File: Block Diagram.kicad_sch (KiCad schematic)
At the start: 0 parts

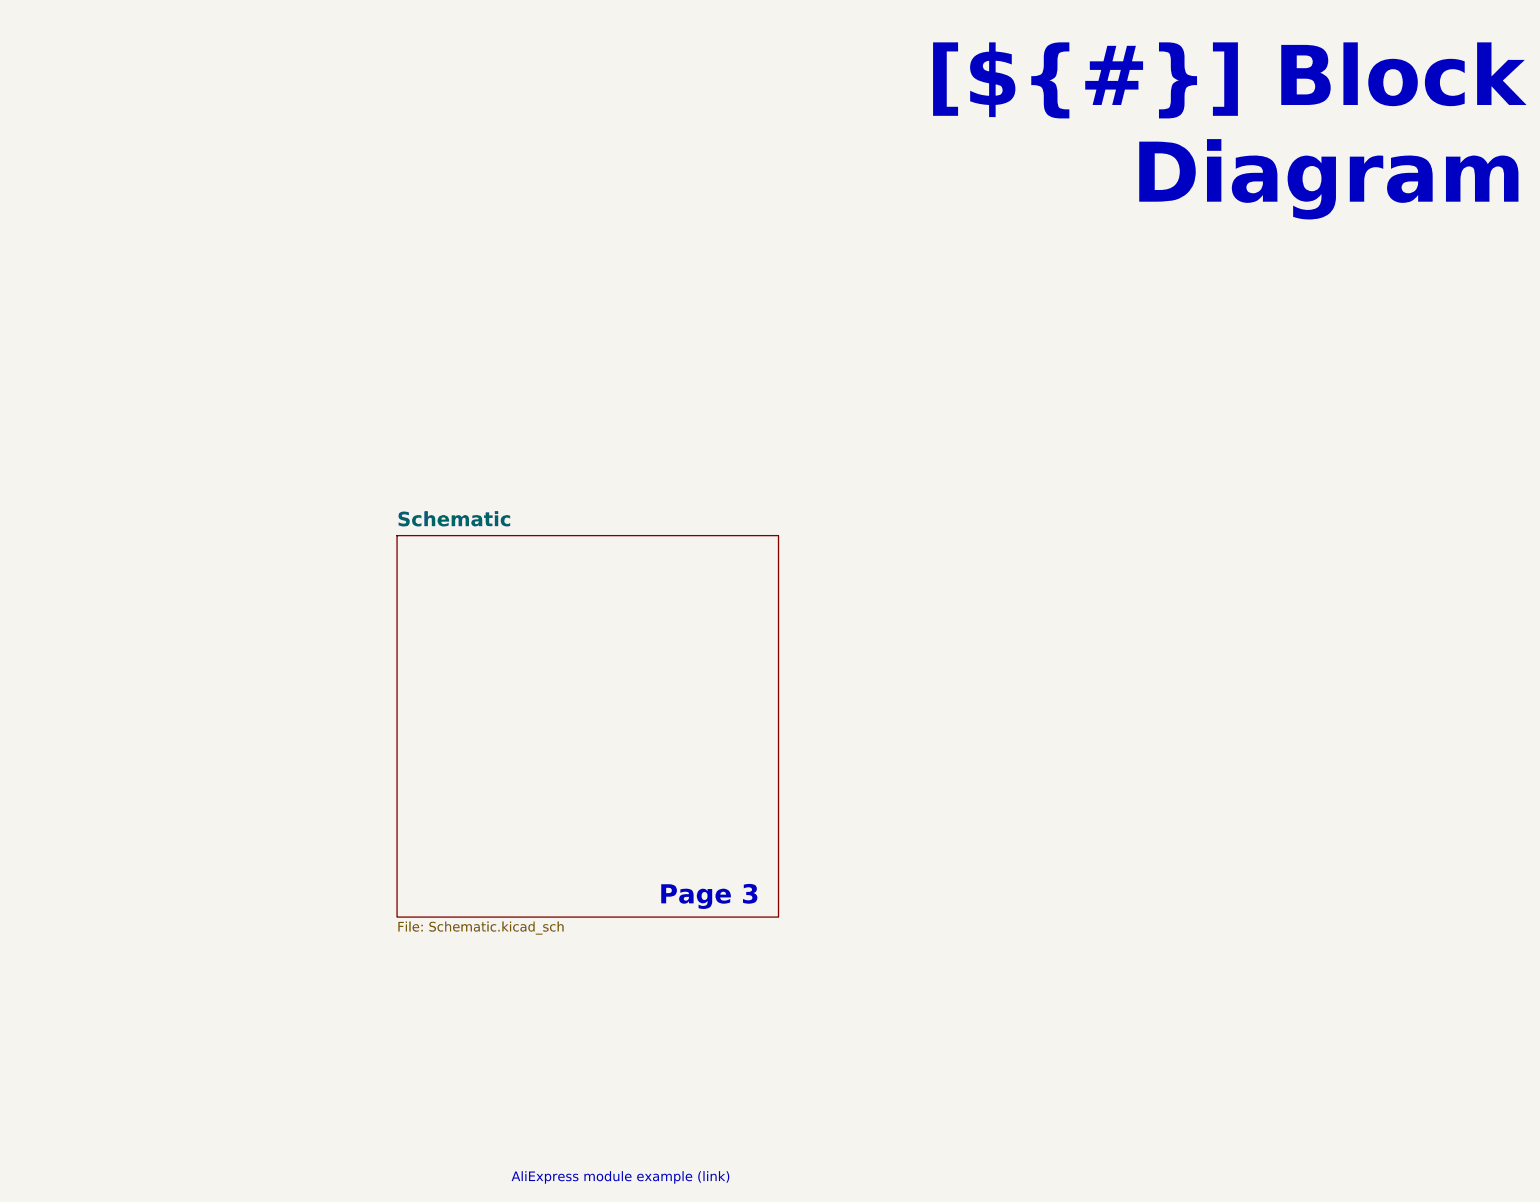
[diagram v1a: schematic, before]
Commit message: added perfboard
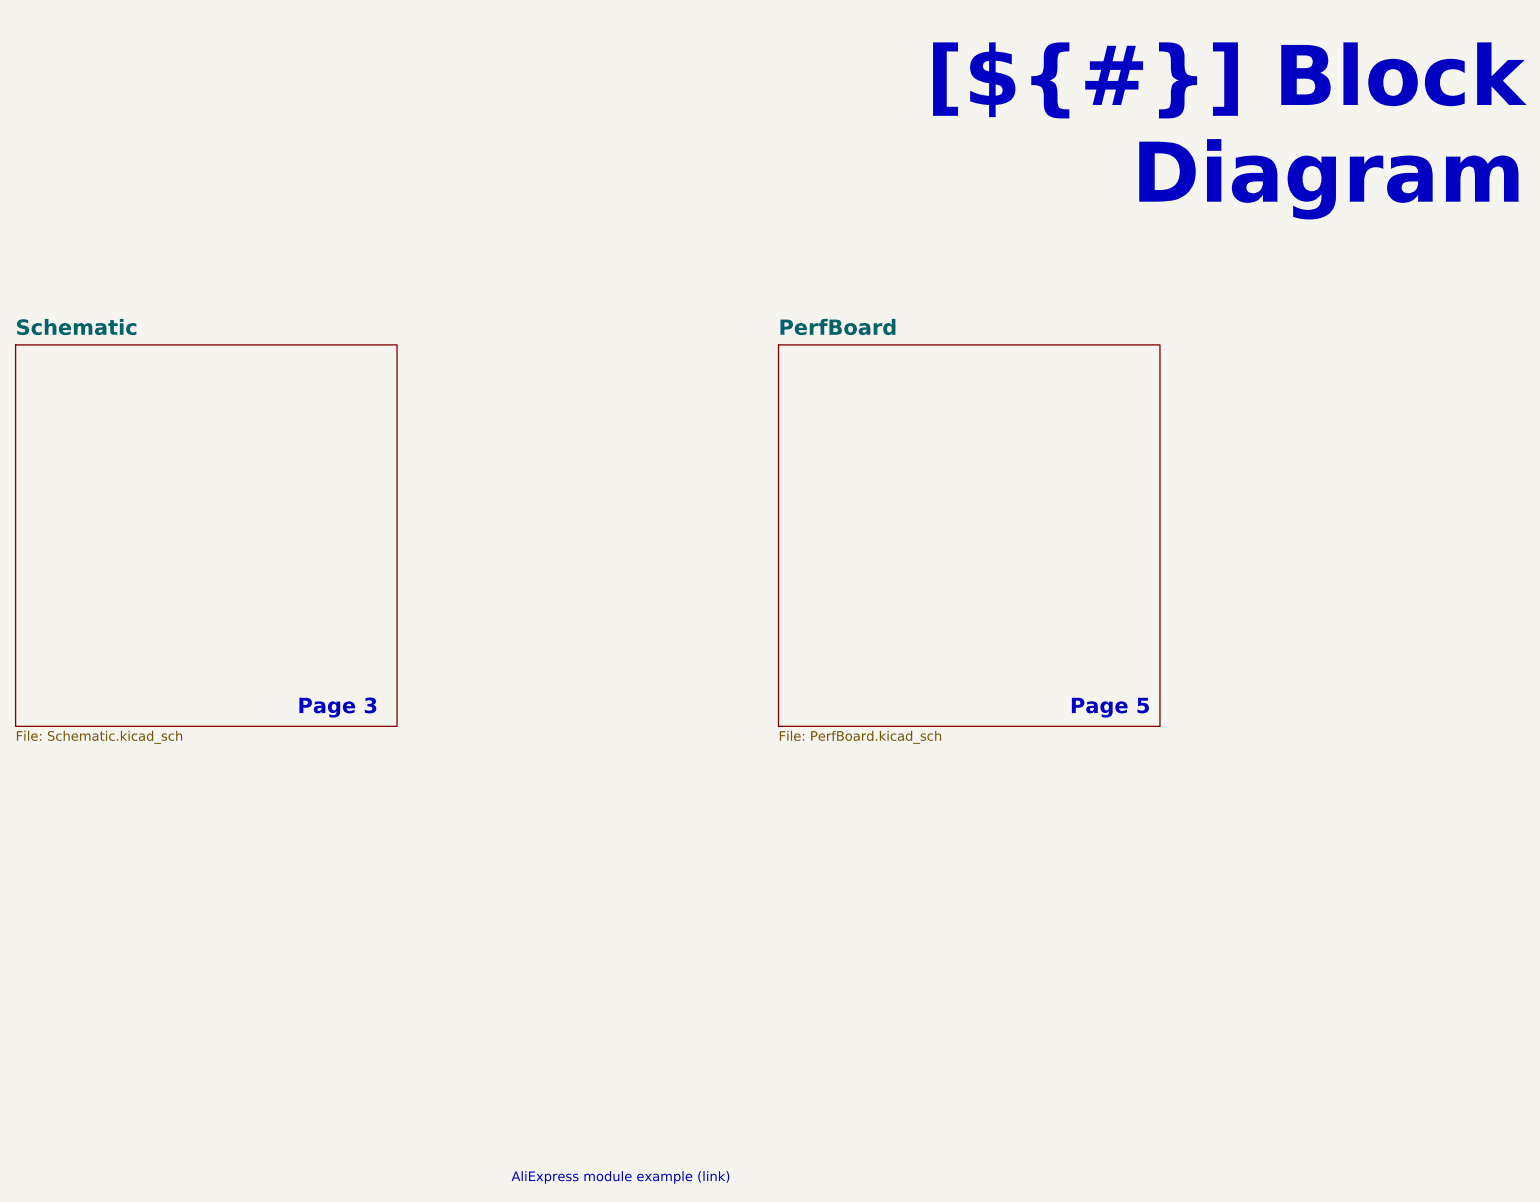
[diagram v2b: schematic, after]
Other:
- added sheet PerfBoard (PerfBoard.kicad_sch)
- note added: "Page 5"
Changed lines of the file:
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@@
 		(comment 9 "FR")
+	)
+	(text "Page 5"
+		(exclude_from_sim no)
+		(at 227.33 100.33 0)
+		(effects
+			(font
+				(size 2.032 2.032)
+				(bold yes)
+				(color 20 60 40 1)
+			)
+			(justify right bottom)
+			(href "#5")
+		)
 	)
 	(text "Page 3"
 		(exclude_from_sim no)
-		(at 175.26 125.73 0)
+		(at 124.46 100.33 0)
 		(effects
 			(font
-				(size 2.54 2.54)
+				(size 2.032 2.032)
 				(bold yes)
 				(color 20 60 40 1)
@@
 	)
 	(sheet
-		(at 127 76.2)
+		(at 177.8 50.8)
+		(size 50.8 50.8)
+		(exclude_from_sim no)
+		(in_bom yes)
+		(on_board yes)
+		(dnp no)
+		(fields_autoplaced yes)
+		(stroke
+			(width 0.1524)
+			(type solid)
+		)
+		(fill
+			(color 128 255 128 0.5020)
+		)
+		(property "Sheetname" "PerfBoard"
+			(at 177.8 49.7074 0)
+			(effects
+				(font
+					(size 2.032 2.032)
+					(thickness 0.4064)
+					(bold yes)
+				)
+				(justify left bottom)
+			)
+		)
+		(property "Sheetfile" "PerfBoard.kicad_sch"
+			(at 177.8 102.1846 0)
+			(effects
+				(font
+					(size 1.27 1.27)
+				)
+				(justify left top)
+			)
+		)
+		(instances
+			(project "Isolated_12to450V"
+				(path "/f9e05184-c88b-4a88-ae9c-ab2bdb32be7c/82da9dbf-ba38-4d08-ba35-a220fa2963b1"
+					(page "5")
+				)
+			)
+		)
+	)
+	(sheet
+		(at 76.2 50.8)
 		(size 50.8 50.8)
 		(exclude_from_sim no)
@@
 		)
 		(property "Sheetname" "Schematic"
-			(at 127 75.1709 0)
+			(at 76.2 49.7074 0)
 			(effects
 				(font
-					(size 1.905 1.905)
+					(size 2.032 2.032)
 					(bold yes)
 				)
@@
 		)
 		(property "Sheetfile" "Schematic.kicad_sch"
-			(at 127 127.5846 0)
+			(at 76.2 102.1846 0)
 			(effects
 				(font

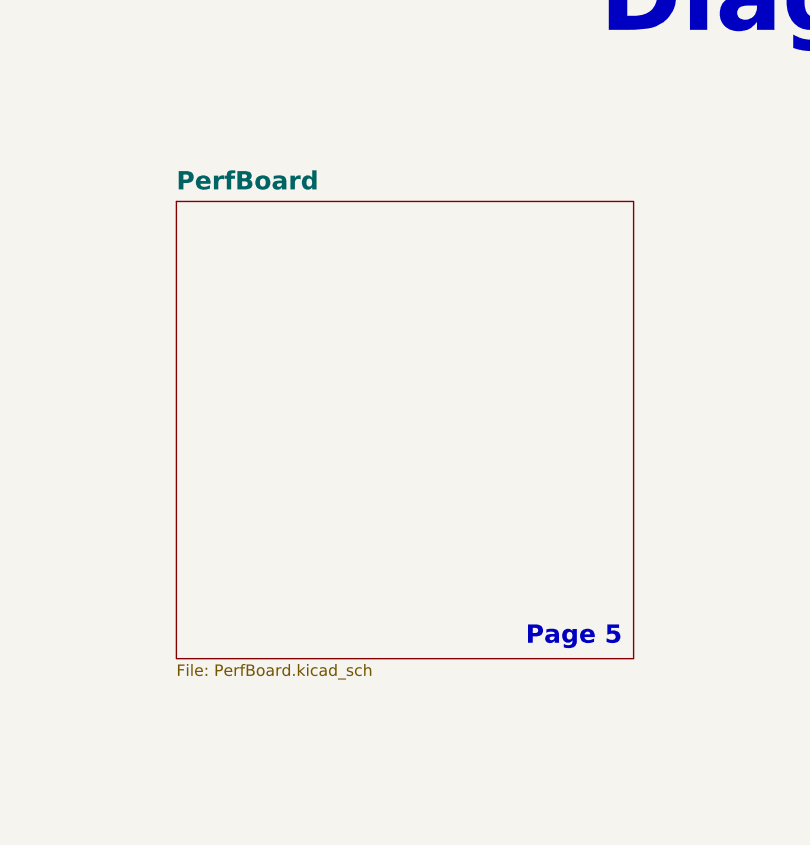
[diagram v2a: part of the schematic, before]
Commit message: Removed perfboard, new branch on linux
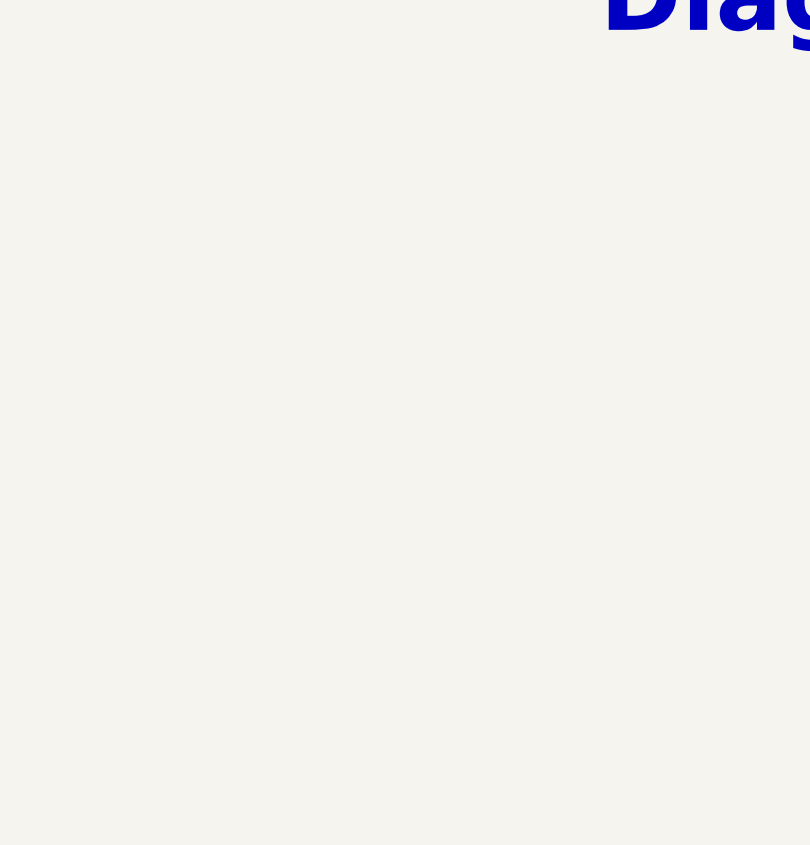
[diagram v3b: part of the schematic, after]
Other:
- removed sheet PerfBoard
- note removed: "Page 5"
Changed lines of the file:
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@@
 		(comment 9 "FR")
-	)
-	(text "Page 5"
-		(exclude_from_sim no)
-		(at 227.33 100.33 0)
-		(effects
-			(font
-				(size 2.032 2.032)
-				(bold yes)
-				(color 20 60 40 1)
-			)
-			(justify right bottom)
-			(href "#5")
-		)
 	)
 	(text "Page 3"
@@
 		)
 	)
-	(sheet
-		(at 177.8 50.8)
-		(size 50.8 50.8)
-		(exclude_from_sim no)
-		(in_bom yes)
-		(on_board yes)
-		(dnp no)
-		(fields_autoplaced yes)
-		(stroke
-			(width 0.1524)
-			(type solid)
-		)
-		(fill
-			(color 128 255 128 0.5020)
-		)
-		(property "Sheetname" "PerfBoard"
-			(at 177.8 49.7074 0)
-			(effects
-				(font
-					(size 2.032 2.032)
-					(thickness 0.4064)
-					(bold yes)
-				)
-				(justify left bottom)
-			)
-		)
-		(property "Sheetfile" "PerfBoard.kicad_sch"
-			(at 177.8 102.1846 0)
-			(effects
-				(font
-					(size 1.27 1.27)
-				)
-				(justify left top)
-			)
-		)
-		(instances
-			(project "Isolated_12to450V"
-				(path "/f9e05184-c88b-4a88-ae9c-ab2bdb32be7c/82da9dbf-ba38-4d08-ba35-a220fa2963b1"
-					(page "5")
-				)
-			)
-		)
-	)
